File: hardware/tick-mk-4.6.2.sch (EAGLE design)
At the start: 31 parts, among them IC1 ATMEGA328P, IC2 DS1307, IC3 L7805, Y1 16MHz, Y2 32.768kHz

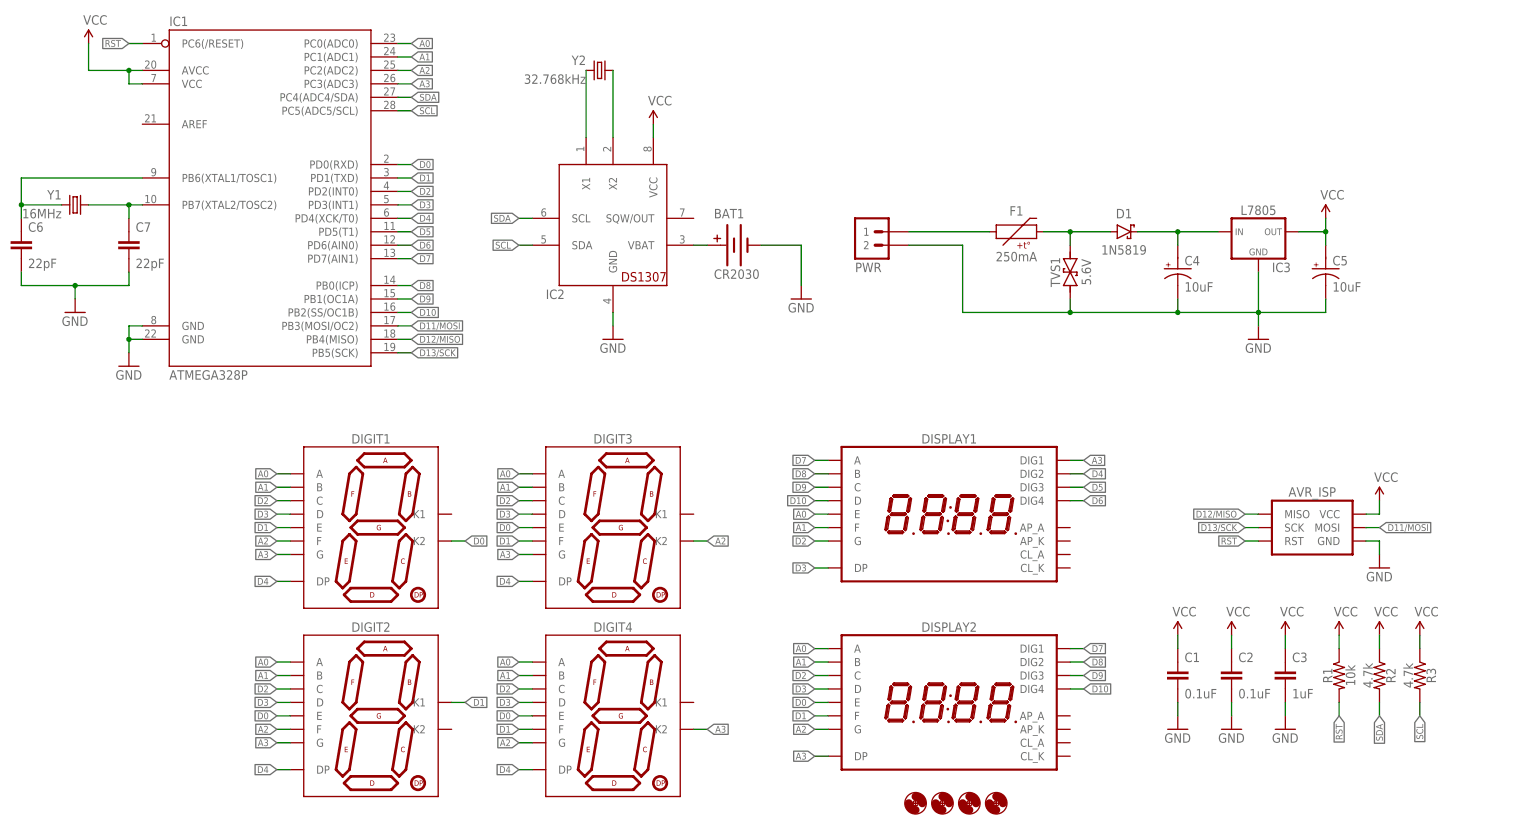
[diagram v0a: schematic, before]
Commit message: nets complete, now for layout
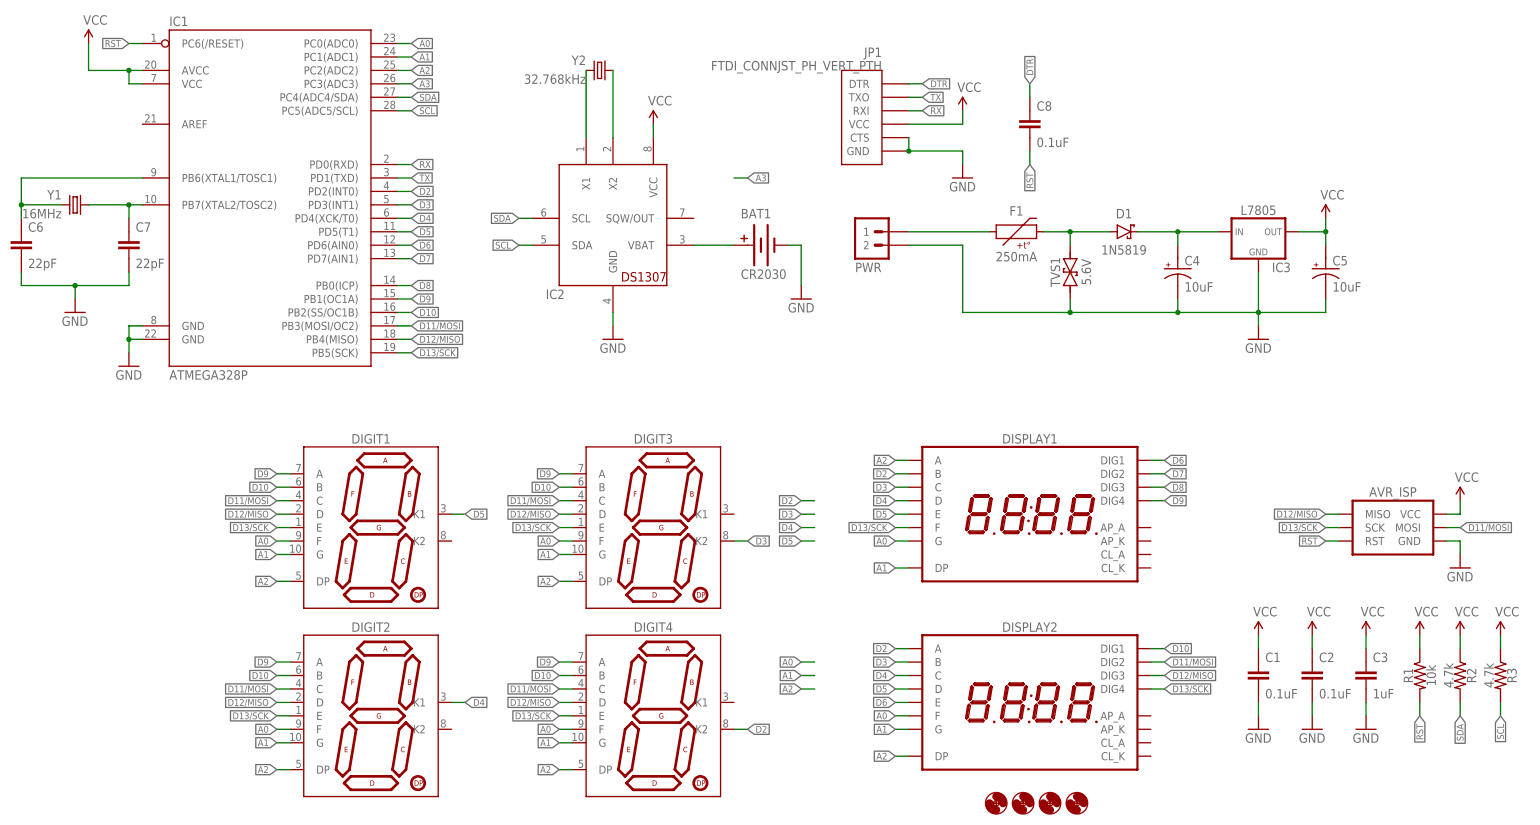
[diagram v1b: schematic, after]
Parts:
- added C8: 0.1uF, A_butts:CAPACITOR-CERAMIC025-024X044
- added JP1: FTDI_CONNJST_PH_VERT_PTH, A_butts:FTDI_CONNJST_PH_VERT_PTH
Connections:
- removed net D0: DIGIT1.K2, DIGIT2.E, DIGIT3.E, DIGIT4.E, DISPLAY2.E, IC1.PD0(RXD)
- removed net D1: DIGIT1.E, DIGIT2.K1, DIGIT3.F, DIGIT4.F, DISPLAY2.F, IC1.PD1(TXD)
- new net DTR: C8.1, JP1.DTR
- new net RX: IC1.PD0(RXD), JP1.RXI
- new net TX: IC1.PD1(TXD), JP1.TXO
- net A0: now also DIGIT1.F, DIGIT2.F, DIGIT3.F, DIGIT4.F, DISPLAY1.G, DISPLAY2.F; no longer DIGIT1.A, DIGIT2.A, DIGIT3.A, DIGIT4.A, DISPLAY1.E, DISPLAY2.A
- net A1: now also DIGIT1.G, DIGIT2.G, DIGIT3.G, DIGIT4.G, DISPLAY1.DP, DISPLAY2.G; no longer DIGIT1.B, DIGIT2.B, DIGIT3.B, DIGIT4.B, DISPLAY1.F, DISPLAY2.B
- net A2: now also DIGIT1.DP, DIGIT2.DP, DIGIT3.DP, DIGIT4.DP, DISPLAY1.A, DISPLAY2.DP; no longer DIGIT1.F, DIGIT2.F, DIGIT3.K2, DIGIT4.G, DISPLAY2.G
- net A3: no longer DIGIT1.G, DIGIT2.G, DIGIT3.G, DIGIT4.K2, DISPLAY1.DIG1, DISPLAY2.DP
- net D10: now also DIGIT1.B, DIGIT2.B, DIGIT3.B, DIGIT4.B, DISPLAY2.DIG1; no longer DISPLAY1.D, DISPLAY2.DIG4
- net D11/MOSI: now also DIGIT1.C, DIGIT2.C, DIGIT3.C, DIGIT4.C, DISPLAY2.DIG2
- net D12/MISO: now also DIGIT1.D, DIGIT2.D, DIGIT3.D, DIGIT4.D, DISPLAY2.DIG3
- net D13/SCK: now also DIGIT1.E, DIGIT2.E, DIGIT3.E, DIGIT4.E, DISPLAY1.F, DISPLAY2.DIG4
- net D2: now also DIGIT4.K2, DISPLAY1.B, DISPLAY2.A; no longer DIGIT1.C, DIGIT2.C, DIGIT3.C, DIGIT4.C, DISPLAY1.G, DISPLAY2.C
- net D3: now also DIGIT3.K2, DISPLAY1.C, DISPLAY2.B; no longer DIGIT1.D, DIGIT2.D, DIGIT3.D, DIGIT4.D, DISPLAY1.DP, DISPLAY2.D
- net D4: now also DIGIT2.K1, DISPLAY1.D, DISPLAY2.C; no longer DIGIT1.DP, DIGIT2.DP, DIGIT3.DP, DIGIT4.DP, DISPLAY1.DIG2
- net D5: now also DIGIT1.K1, DISPLAY1.E, DISPLAY2.D; no longer DISPLAY1.DIG3
- net D6: now also DISPLAY1.DIG1, DISPLAY2.E; no longer DISPLAY1.DIG4
- net D7: now also DISPLAY1.DIG2; no longer DISPLAY1.A, DISPLAY2.DIG1
- net D8: now also DISPLAY1.DIG3; no longer DISPLAY1.B, DISPLAY2.DIG2
- net D9: now also DIGIT1.A, DIGIT2.A, DIGIT3.A, DIGIT4.A, DISPLAY1.DIG4; no longer DISPLAY1.C, DISPLAY2.DIG3
- net GND: now also JP1.CTS, JP1.GND
- net RST: now also C8.2
- net VCC: now also JP1.VCC
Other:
- note added: "D11"
- note added: "D12"
- note added: "D13"
- note removed: "A3"
- note removed: "D0"
- note removed: "D1"
- note removed: "Display1"
- note removed: "Display2"
- note removed: "digit1"
- note removed: "digit2"
- note removed: "digit3"
- note removed: "digit4"
- moved on the sheet: AVR_ISP, BAT1, C1, C2, C3, DISPLAY1, DISPLAY2, R1, R2, R3

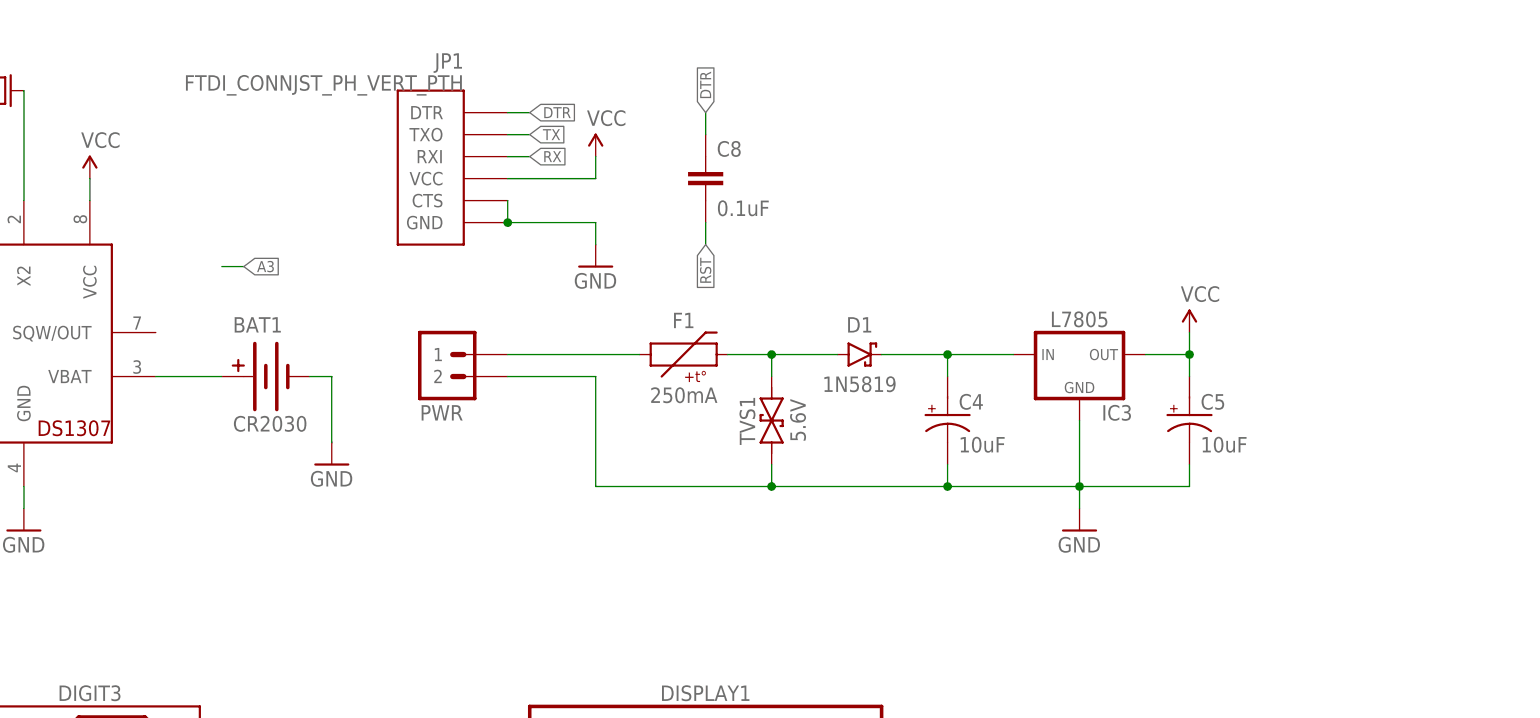
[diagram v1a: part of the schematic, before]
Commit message: layout done but still need to add battery monitoring circuit
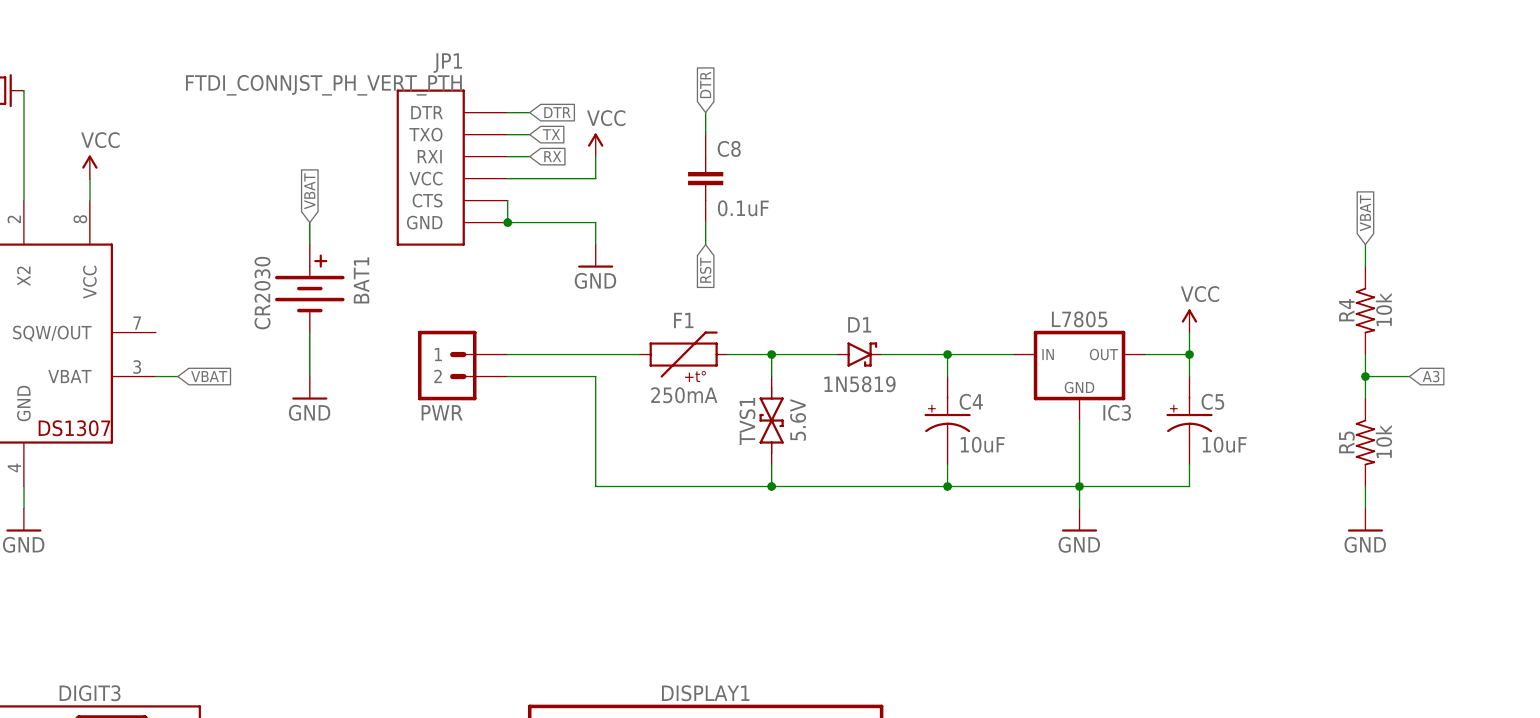
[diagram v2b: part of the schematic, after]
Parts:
- added R4, R5: 10k, A_butts:RESISTORPTH-AXIAL-7.62MM
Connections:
- removed net N$1: BAT1.+, IC2.VBAT
- new net VBAT: BAT1.+, IC2.VBAT, R4.1
- net A3: now also R4.2, R5.1
- net GND: now also R5.2
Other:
- moved on the sheet: BAT1
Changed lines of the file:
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@@
 <layer number="56" name="wert" color="7" fill="1" visible="yes" active="no"/>
 <layer number="57" name="tCAD" color="7" fill="1" visible="yes" active="no"/>
+<layer number="90" name="Modules" color="5" fill="1" visible="yes" active="yes"/>
 <layer number="91" name="Nets" color="2" fill="1" visible="yes" active="yes"/>
 <layer number="92" name="Busses" color="1" fill="1" visible="yes" active="yes"/>
@@
 <part name="GND3" library="A_butts" deviceset="GND" device=""/>
 <part name="C8" library="A_butts" deviceset="CAPACITOR-CERAMIC" device="025-024X044" value="0.1uF"/>
+<part name="R4" library="A_butts" deviceset="RESISTOR" device="PTH-AXIAL-7.62MM" value="10k"/>
+<part name="R5" library="A_butts" deviceset="RESISTOR" device="PTH-AXIAL-7.62MM" value="10k"/>
+<part name="GND6" library="A_butts" deviceset="GND" device=""/>
 </parts>
 <sheets>
@@
 <instance part="IC3" gate="G$1" x="246.38" y="119.38"/>
 <instance part="D1" gate="G$1" x="220.98" y="119.38"/>
-<instance part="BAT1" gate="G$1" x="152.4" y="116.84"/>
-<instance part="GND1" gate="1" x="160.02" y="106.68"/>
+<instance part="BAT1" gate="G$1" x="157.48" y="127" rot="R270"/>
+<instance part="GND1" gate="1" x="157.48" y="114.3"/>
 <instance part="Y1" gate="G$1" x="22.86" y="124.46" rot="MR0"/>
 <instance part="C6" gate="G$1" x="12.7" y="116.84"/>
@@
 <instance part="GND3" gate="1" x="190.5" y="129.54"/>
 <instance part="C8" gate="G$1" x="203.2" y="139.7"/>
+<instance part="R4" gate="G$1" x="279.4" y="124.46" rot="MR270"/>
+<instance part="R5" gate="G$1" x="279.4" y="109.22" rot="MR270"/>
+<instance part="GND6" gate="1" x="279.4" y="99.06"/>
 </instances>
 <busses>
@@
 </segment>
 <segment>
-<wire x1="147.32" y1="129.54" x2="149.86" y2="129.54" width="0.1524" layer="91"/>
-<label x="149.86" y="129.54" size="1.27" layer="95" rot="MR180" xref="yes"/>
+<label x="284.48" y="116.84" size="1.27" layer="95" rot="MR180" xref="yes"/>
+<pinref part="R5" gate="G$1" pin="1"/>
+<pinref part="R4" gate="G$1" pin="2"/>
+<wire x1="279.4" y1="114.3" x2="279.4" y2="116.84" width="0.1524" layer="91"/>
+<wire x1="279.4" y1="116.84" x2="279.4" y2="119.38" width="0.1524" layer="91"/>
+<wire x1="284.48" y1="116.84" x2="279.4" y2="116.84" width="0.1524" layer="91"/>
+<junction x="279.4" y="116.84"/>
 </segment>
 </net>
@@
 <segment>
 <pinref part="BAT1" gate="G$1" pin="-"/>
-<wire x1="157.48" y1="116.84" x2="160.02" y2="116.84" width="0.1524" layer="91"/>
 <pinref part="GND1" gate="1" pin="GND"/>
-<wire x1="160.02" y1="116.84" x2="160.02" y2="109.22" width="0.1524" layer="91"/>
+<wire x1="157.48" y1="121.92" x2="157.48" y2="116.84" width="0.1524" layer="91"/>
 </segment>
 <segment>
@@
 <junction x="180.34" y="134.62"/>
 </segment>
+<segment>
+<pinref part="R5" gate="G$1" pin="2"/>
+<wire x1="279.4" y1="101.6" x2="279.4" y2="104.14" width="0.1524" layer="91"/>
+<pinref part="GND6" gate="1" pin="GND"/>
+</segment>
 </net>
 <net name="RST" class="0">
@@
 <junction x="210.82" y="119.38"/>
 <pinref part="F1" gate="G$1" pin="2"/>
-</segment>
-</net>
-<net name="N$1" class="0">
-<segment>
-<pinref part="BAT1" gate="G$1" pin="+"/>
-<wire x1="147.32" y1="116.84" x2="139.7" y2="116.84" width="0.1524" layer="91"/>
-<pinref part="IC2" gate="G$1" pin="VBAT"/>
 </segment>
 </net>
@@
 </segment>
 </net>
+<net name="VBAT" class="0">
+<segment>
+<pinref part="IC2" gate="G$1" pin="VBAT"/>
+<wire x1="142.24" y1="116.84" x2="139.7" y2="116.84" width="0.1524" layer="91"/>
+<label x="142.24" y="116.84" size="1.27" layer="95" xref="yes"/>
+</segment>
+<segment>
+<pinref part="BAT1" gate="G$1" pin="+"/>
+<wire x1="157.48" y1="132.08" x2="157.48" y2="134.62" width="0.1524" layer="91"/>
+<label x="157.48" y="134.62" size="1.27" layer="95" rot="R90" xref="yes"/>
+</segment>
+<segment>
+<pinref part="R4" gate="G$1" pin="1"/>
+<wire x1="279.4" y1="132.08" x2="279.4" y2="129.54" width="0.1524" layer="91"/>
+<label x="279.4" y="132.08" size="1.27" layer="95" rot="R90" xref="yes"/>
+</segment>
+</net>

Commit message: resistor divider to check battery level
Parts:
- R4, R5: device A_butts:RESISTORPTH-AXIAL-7.62MM -> A_butts:RESISTORPTH-AXIAL-6.35MM
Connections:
- net A3: now also R5.2; no longer R5.1
- net GND: now also R5.1; no longer R5.2
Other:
- moved on the sheet: R5
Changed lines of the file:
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@@
 <part name="GND3" library="A_butts" deviceset="GND" device=""/>
 <part name="C8" library="A_butts" deviceset="CAPACITOR-CERAMIC" device="025-024X044" value="0.1uF"/>
-<part name="R4" library="A_butts" deviceset="RESISTOR" device="PTH-AXIAL-7.62MM" value="10k"/>
-<part name="R5" library="A_butts" deviceset="RESISTOR" device="PTH-AXIAL-7.62MM" value="10k"/>
+<part name="R4" library="A_butts" deviceset="RESISTOR" device="PTH-AXIAL-6.35MM" value="10k"/>
+<part name="R5" library="A_butts" deviceset="RESISTOR" device="PTH-AXIAL-6.35MM" value="10k"/>
 <part name="GND6" library="A_butts" deviceset="GND" device=""/>
 </parts>
@@
 <instance part="C8" gate="G$1" x="203.2" y="139.7"/>
 <instance part="R4" gate="G$1" x="279.4" y="124.46" rot="MR270"/>
-<instance part="R5" gate="G$1" x="279.4" y="109.22" rot="MR270"/>
+<instance part="R5" gate="G$1" x="279.4" y="109.22" rot="R90"/>
 <instance part="GND6" gate="1" x="279.4" y="99.06"/>
 </instances>
@@
 <segment>
 <label x="284.48" y="116.84" size="1.27" layer="95" rot="MR180" xref="yes"/>
-<pinref part="R5" gate="G$1" pin="1"/>
+<pinref part="R5" gate="G$1" pin="2"/>
 <pinref part="R4" gate="G$1" pin="2"/>
 <wire x1="279.4" y1="114.3" x2="279.4" y2="116.84" width="0.1524" layer="91"/>
@@
 </segment>
 <segment>
-<pinref part="R5" gate="G$1" pin="2"/>
+<pinref part="R5" gate="G$1" pin="1"/>
 <wire x1="279.4" y1="101.6" x2="279.4" y2="104.14" width="0.1524" layer="91"/>
 <pinref part="GND6" gate="1" pin="GND"/>
